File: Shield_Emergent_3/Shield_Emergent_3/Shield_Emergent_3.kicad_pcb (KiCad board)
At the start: 4 copper layers, 23.6 x 33.4 mm, 29 parts, among them J1 USB3_B_Micro, J2 Conn_01x04_Socket, J3 USB3_B_Micro, J4 Conn_01x05, J5 Conn_01x02_Socket, J6 Conn_01x02_Socket, J7 Conn_01x05, J9 Conn_01x10, U3 SP3012-06UTG, U4 SP3012-06UTG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

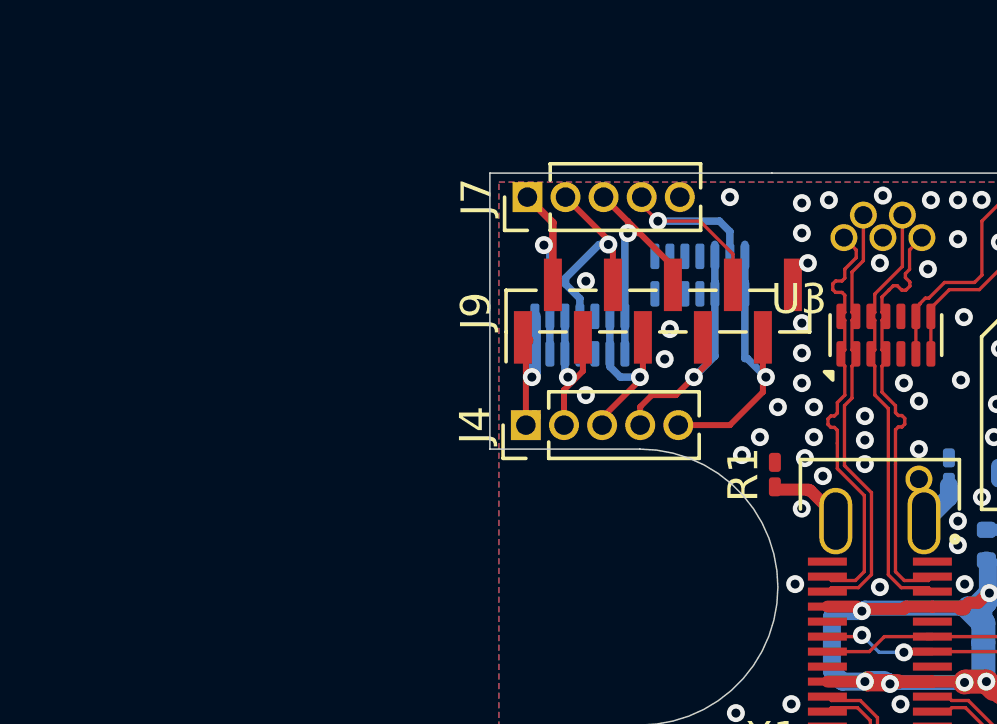
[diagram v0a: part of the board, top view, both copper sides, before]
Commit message: v2.1 prothos 4 15-pin connector
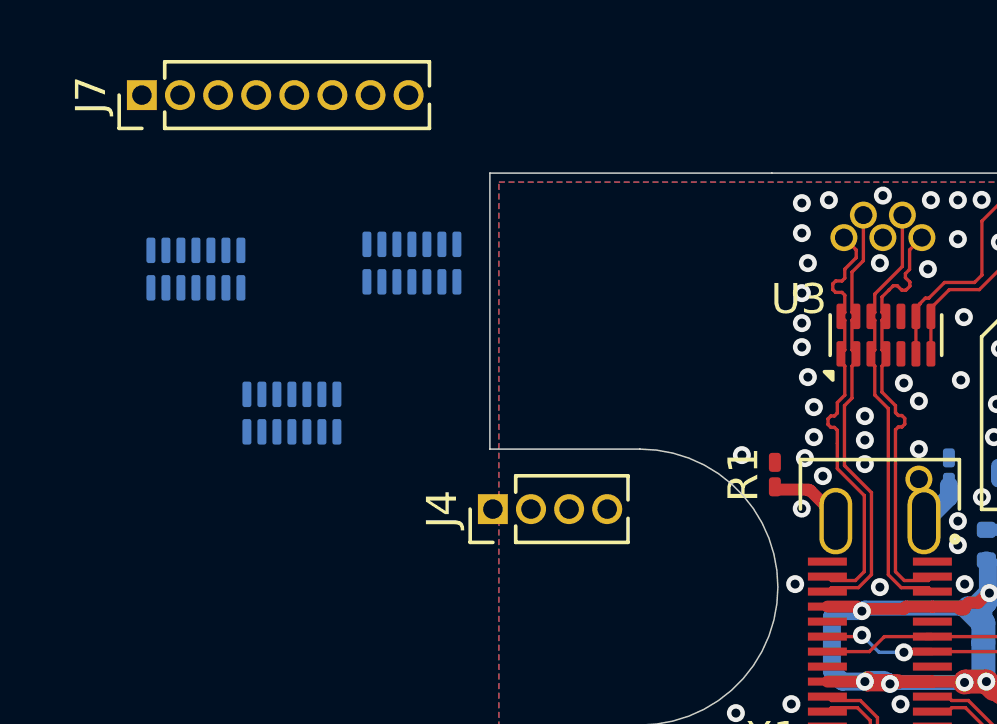
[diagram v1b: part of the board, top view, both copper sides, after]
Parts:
- removed J9: Conn_01x10, Connector_PinHeader_1.00mm:PinHeader_1x10_P1.00mm_Vertical_SMD_Pin1Left
- added U7: SP3012-06UTG, myLib8:DFN-14_1.35x3.5mm_P0.5mm, B.Cu at (-0.40, 3.20)
- J4: value Conn_01x05 -> Conn_01x07; footprint Connector_PinHeader_1.27mm:PinHeader_1x05_P1.27mm_Vertical -> Connector_PinHeader_1.27mm:PinHeader_1x04_P1.27mm_Vertical
- J7: value Conn_01x05 -> Conn_01x08; footprint Connector_PinHeader_1.27mm:PinHeader_1x05_P1.27mm_Vertical -> Connector_PinHeader_1.27mm:PinHeader_1x08_P1.27mm_Vertical
- moved U6 16.8 mm to (-7.60, 3.40)
- moved J7 13.3 mm to (-9.40, -2.40)
- moved U5 9.95 mm to (-4.40, 8.20)
- moved J4 3.01 mm to (2.30, 11.4)
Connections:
- J4 pad 2: K3 -> K2
- J4 pad 3: K5 -> K3
- J4 pad 4: K7 -> K4
- J7 pad 1: K2 -> K8
- J7 pad 2: K4 -> K9
- J7 pad 3: K6 -> K10
- J7 pad 4: K8 -> K11
- J7 pad 5: GND -> K12
- U6 pad 6: unconnected-(U6-Pad6) -> K10
- U6 pad 7: unconnected-(U6-Pad7) -> K11
- U6 pad 8: unconnected-(U6-Pad8) -> K11
- U6 pad 9: unconnected-(U6-Pad9) -> K10
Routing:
- net K9: track 9.95 -> 0.00 mm, vias 1 -> 0
- net K8: track 9.22 -> 0.00 mm, vias 1 -> 0
- net K6: track 8.88 -> 0.00 mm, vias 1 -> 0
- net K7: track 8.88 -> 0.00 mm, vias 1 -> 0
- net K4: track 8.20 -> 0.00 mm, vias 1 -> 0
- net K2: track 6.98 -> 0.00 mm, vias 1 -> 0
- net K5: track 6.73 -> 0.00 mm, vias 1 -> 0
- net K1: track 5.46 -> 0.00 mm, vias 1 -> 0
- net K3: track 5.44 -> 0.00 mm, vias 1 -> 0
- net GND: vias 140 -> 134
